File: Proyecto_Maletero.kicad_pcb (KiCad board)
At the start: 2 copper layers, 65.2 x 59 mm, 50 parts, among them J1 DE9_Pins, J2 Conn_01x02, J3 Conn_01x02, J4 Conn_01x03, J5 Conn_01x02, J6 DE9_Pins, J7 Conn_01x04, J9 Conn_01x04, K1 FINDER-34.51, Q2 MMBT5550L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

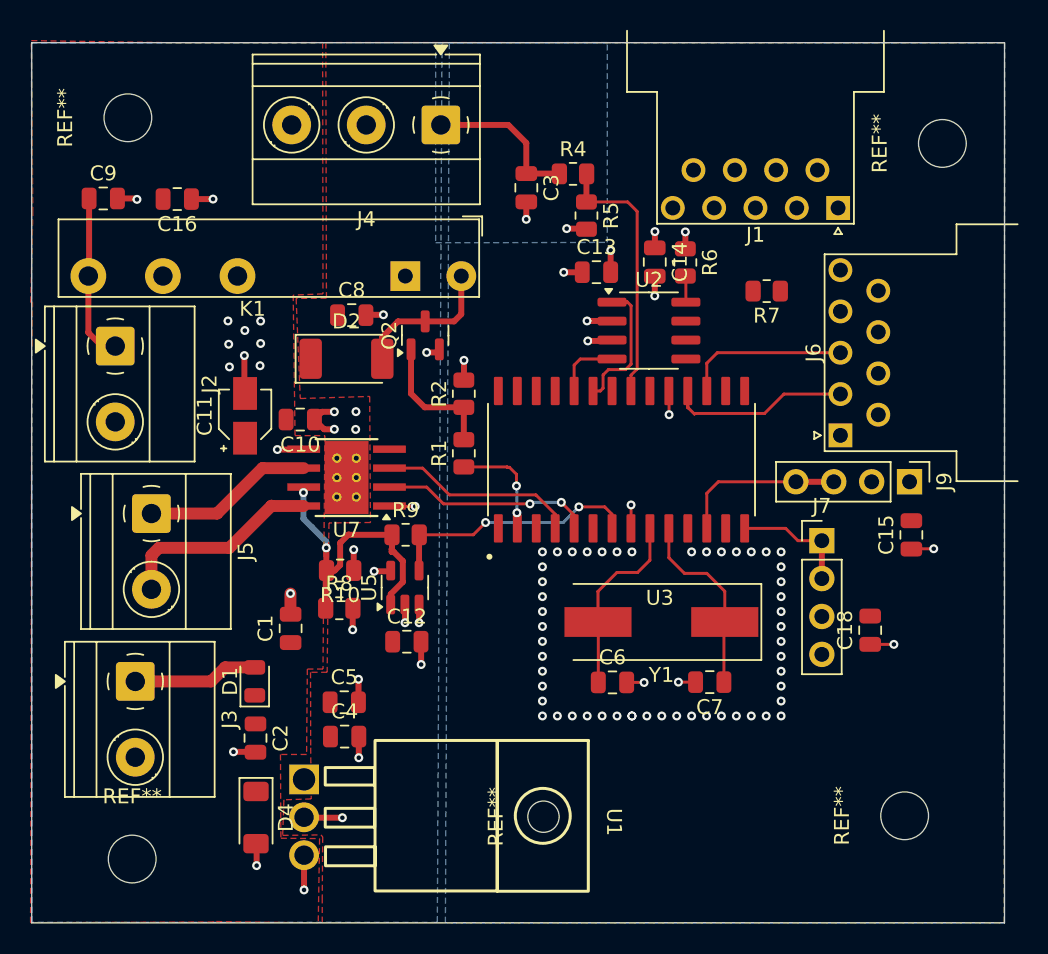
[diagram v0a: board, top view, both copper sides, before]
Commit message: Reglas de diseño, errores 0, separación del transcriver
hay 108 warnings igualmente
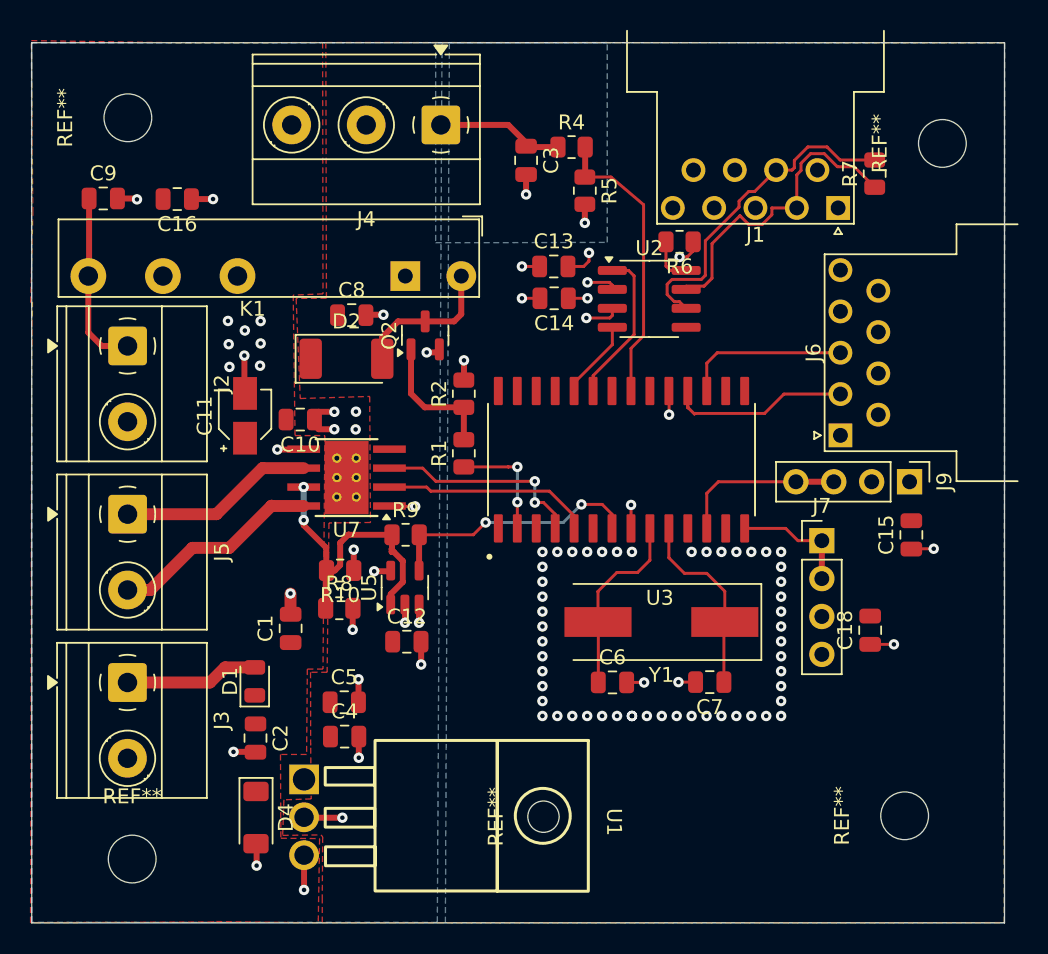
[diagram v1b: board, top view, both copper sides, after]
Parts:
- moved R7 10.7 mm to (165.0, 93.0), turned to 90 degrees
- moved C14 7.17 mm to (143.5, 101.3), turned to 180 degrees
- moved C13 2.89 mm to (143.5, 99.2)
- moved U2 2.12 mm to (149.9, 101.4)
- moved C3 1.84 mm to (141.6, 92.1)
- moved R4 1.80 mm to (144.7, 91.2)
- moved R5 1.67 mm to (145.5, 94.1)
- moved J5 1.60 mm to (114.9, 115.8)
- moved R6 1.43 mm to (151.9, 97.5), turned to 180 degrees
- moved J2 0.82 mm to (114.9, 104.5)
- moved J3 0.53 mm to (114.9, 127.1)
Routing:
- net CAN-: track 0.00 -> 22.3 mm
- net CAN+: track 0.00 -> 21.2 mm
- net Sensor_Pie_12V: track 10.5 -> 8.61 mm
- net Sensor_Pie: track 17.8 -> 19.5 mm
- net Motor+: track 11.5 -> 13.1 mm
- net CAN_TX: track 9.39 -> 10.7 mm
- net Net-(U2-Rs): track 1.80 -> 3.10 mm
- net VCC: track 8.15 -> 9.33 mm
- net GND: track 15.1 -> 16.1 mm
- net CAN_RX: track 4.44 -> 5.33 mm
- net PH_A: track 13.3 -> 14.2 mm, vias 0 -> 2
- net VRth: track 11.2 -> 12.0 mm
- net VBATERIA: track 8.40 -> 8.95 mm
- net PH_B: track 14.1 -> 14.0 mm, vias 2 -> 0

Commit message: Algun cambio
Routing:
- net CAN+: track 21.2 -> 17.4 mm
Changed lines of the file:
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@@
 		(tags "capacitor")
 		(property "Reference" "C16"
-			(at 0 -1.68 0)
+			(at 0 1.82 0)
 			(layer "F.SilkS")
 			(effects
@@
 		(tags "capacitor")
 		(property "Reference" "C3"
-			(at 0 -1.68 90)
+			(at 0.045 1.575 90)
 			(layer "F.SilkS")
 			(effects
@@
 		)
 		(property "Value" "LM1084-5.0"
-			(at 0 1 270)
+			(at 0 0.88 270)
 			(unlocked yes)
 			(layer "F.Fab")
@@
 		(tags "resistor")
 		(property "Reference" "R6"
-			(at 0 -1.65 0)
+			(at -2.568 0.046 0)
 			(layer "F.SilkS")
 			(effects
@@
 		(tags "capacitor")
 		(property "Reference" "C7"
-			(at 0 -1.68 0)
+			(at -2.645 -0.04 0)
 			(layer "F.SilkS")
 			(effects
@@
 		(tags "capacitor")
 		(property "Reference" "C2"
-			(at 0 -1.68 90)
+			(at -0.01 -1.545 90)
 			(layer "F.SilkS")
 			(effects
@@
 		(tags "capacitor")
 		(property "Reference" "C12"
-			(at 0 -1.68 0)
+			(at -0.58 1.83 0)
 			(layer "F.SilkS")
 			(effects
@@
 		(tags "resistor")
 		(property "Reference" "R8"
-			(at 0 -1.65 0)
+			(at 0.0575 1.49 0)
 			(layer "F.SilkS")
 			(effects
@@
 		(tags "SOT TO_SOT_SMD")
 		(property "Reference" "U5"
-			(at 0 -2.4 90)
+			(at 0 -1.56 90)
 			(layer "F.SilkS")
 			(effects
@@
 		(tags "resistor")
 		(property "Reference" "R9"
-			(at 0 -1.65 0)
+			(at 2.5925 0.995 0)
 			(layer "F.SilkS")
 			(effects
@@
 		(tags "THT Terminal Block Phoenix MKDS-1,5-3 pitch 5mm size 15x9.8mm drill 1.3mm pad 2.6mm")
 		(property "Reference" "J4"
-			(at 5 -6.32 0)
+			(at -3.57 2.37 0)
 			(layer "F.SilkS")
 			(effects
@@
 		(tags "Capacitor Electrolytic")
 		(property "Reference" "C11"
-			(at 0 -2.7 90)
+			(at -3.62 -1.015 90)
 			(layer "F.SilkS")
 			(effects
@@
 		(tags "capacitor")
 		(property "Reference" "C6"
-			(at 0 -1.68 0)
+			(at -2.705 0.02 0)
 			(layer "F.SilkS")
 			(effects
@@
 		(tags "resistor")
 		(property "Reference" "R10"
-			(at 0 -1.65 0)
+			(at 3.13 0.12 0)
 			(layer "F.SilkS")
 			(effects
@@
 		(tags "SOIC SO")
 		(property "Reference" "U2"
-			(at 0 -3.4 0)
+			(at -0.42 -3.3502 0)
 			(layer "F.SilkS")
 			(effects
@@
 		(tags "resistor")
 		(property "Reference" "R7"
-			(at 0 -1.65 90)
+			(at -2.756 0.117 90)
 			(layer "F.SilkS")
 			(effects
@@
 		(tags "capacitor")
 		(property "Reference" "C18"
-			(at 0 -1.68 90)
+			(at -3.52 0 90)
 			(layer "F.SilkS")
 			(effects
@@
 		(tags "capacitor")
 		(property "Reference" "C4"
-			(at 0 -1.68 0)
+			(at -2.28 -0.01 90)
 			(layer "F.SilkS")
 			(effects
@@
 	)
 	(segment
-		(start 155.942174 95.784554)
-		(end 156.52395 96.366331)
-		(width 0.2)
-		(layer "F.Cu")
-		(net 8)
-	)
-	(segment
-		(start 154.06798 97.658748)
-		(end 155.942174 95.784554)
-		(width 0.2)
-		(layer "F.Cu")
-		(net 8)
-	)
-	(segment
-		(start 153.537356 100.50618)
-		(end 154.06798 99.975556)
+		(start 160.88 95.23)
+		(end 159.785331 95.23)
 		(width 0.2)
 		(layer "F.Cu")
@@
 	)
 	(segment
-		(start 160.034 92.269281)
-		(end 160.034 92.75953)
+		(start 161.706831 93.8765)
+		(end 161.11 94.473331)
 		(width 0.2)
 		(layer "F.Cu")
@@
 	)
 	(segment
-		(start 160.034 92.75953)
-		(end 159.75 93.04353)
+		(start 154.06798 97.658748)
+		(end 154.06798 100.39202)
 		(width 0.2)
 		(layer "F.Cu")
@@
 	)
 	(segment
-		(start 156.52395 96.366331)
-		(end 157.43605 96.366331)
+		(start 159.785331 95.23)
+		(end 159.75 95.265331)
 		(width 0.2)
 		(layer "F.Cu")
@@
 	)
 	(segment
-		(start 161.59105 91.624331)
-		(end 160.67895 91.624331)
+		(start 161.11 94.473331)
+		(end 161.11 95)
 		(width 0.2)
 		(layer "F.Cu")
@@
 	)
 	(segment
-		(start 152.335 100.7252)
-		(end 152.335 100.50618)
+		(start 161.11 95)
+		(end 160.88 95.23)
 		(width 0.2)
 		(layer "F.Cu")
@@
 	)
 	(segment
-		(start 159.75 93.04353)
-		(end 159.75 95.265331)
+		(start 164.973 93.8765)
+		(end 161.706831 93.8765)
 		(width 0.2)
 		(layer "F.Cu")
@@
 	)
 	(segment
-		(start 158.081 95.721381)
-		(end 158.081 95.265331)
+		(start 155.360397 96.366331)
+		(end 154.06798 97.658748)
 		(width 0.2)
 		(layer "F.Cu")
@@
 	)
 	(segment
-		(start 163.598001 92.501501)
-		(end 162.46822 92.501501)
+		(start 157.543669 96.366331)
+		(end 158.68 95.23)
 		(width 0.2)
 		(layer "F.Cu")
@@
 	)
 	(segment
-		(start 160.67895 91.624331)
-		(end 160.034 92.269281)
+		(start 153.6148 100.7252)
+		(end 152.335 100.7252)
 		(width 0.2)
 		(layer "F.Cu")
@@
 	)
 	(segment
-		(start 164.973 93.8765)
-		(end 163.598001 92.501501)
+		(start 157.543669 96.366331)
+		(end 155.360397 96.366331)
 		(width 0.2)
 		(layer "F.Cu")
@@
 	)
 	(segment
-		(start 154.06798 99.975556)
-		(end 154.06798 97.658748)
+		(start 153.74 100.72)
+		(end 153.62 100.72)
 		(width 0.2)
 		(layer "F.Cu")
@@
 	)
 	(segment
-		(start 157.43605 96.366331)
-		(end 158.081 95.721381)
+		(start 154.06798 100.39202)
+		(end 153.74 100.72)
 		(width 0.2)
 		(layer "F.Cu")
@@
 	)
 	(segment
-		(start 152.335 100.50618)
-		(end 153.537356 100.50618)
+		(start 158.68 95.23)
+		(end 159.714669 95.23)
 		(width 0.2)
 		(layer "F.Cu")
@@
 	)
 	(segment
-		(start 162.46822 92.501501)
-		(end 161.59105 91.624331)
-		(width 0.2)
-		(layer "F.Cu")
-		(net 8)
-	)
-	(segment
-		(start 158.081 95.265331)
+		(start 159.714669 95.23)
 		(end 159.75 95.265331)
 		(width 0.2)
@@
 	)
 	(segment
-		(start 153.618 99.789168)
-		(end 153.618 97.472331)
-		(width 0.2)
-		(layer "F.Cu")
-		(net 12)
-	)
-	(segment
-		(start 159.58402 92.573112)
-		(end 159.431801 92.725331)
+		(start 153.62 100.72)
+		(end 153.6148 100.7252)
 		(width 0.2)
 		(layer "F.Cu")
-		(net 12)
+		(net 8)
 	)
 	(segment
-		(start 152.335 101.9952)
-		(end 151.885 101.5452)
+		(start 160.67895 91.624331)
+		(end 161.734331 91.624331)
 		(width 0.2)
 		(layer "F.Cu")
@@
 	)
 	(segment
-		(start 161.777438 91.174351)
-		(end 160.492562 91.174351)
+		(start 153.618 97.472331)
+		(end 155.51 95.580331)
 		(width 0.2)
 		(layer "F.Cu")
@@
 	)
 	(segment
-		(start 151.387032 100.0562)
-		(end 153.350968 100.0562)
+		(start 161.734331 91.624331)
+		(end 162.1615 92.0515)
 		(width 0.2)
 		(layer "F.Cu")
@@
 	)
 	(segment
-		(start 153.350968 100.0562)
-		(end 153.618 99.789168)
+		(start 151.059 101.789)
+		(end 151.27 102)
 		(width 0.2)
 		(layer "F.Cu")
@@
 	)
 	(segment
-		(start 151.059 100.384232)
-		(end 151.387032 100.0562)
-		(width 0.2)
-		(layer "F.Cu")
-		(net 12)
-	)
-	(segment
-		(start 156.52395 94.164331)
-		(end 156.926 94.164331)
+		(start 157.254669 92.725331)
+		(end 158.365 92.725331)
 		(width 0.2)
 		(layer "F.Cu")
@@
 	)
 	(segment
-		(start 153.618 97.472331)
-		(end 155.879 95.211331)
+		(start 151.387032 100.0562)
+		(end 151.059 100.384232)
 		(width 0.2)
 		(layer "F.Cu")
@@
 	)
 	(segment
-		(start 151.885 101.5452)
-		(end 151.538032 101.5452)
+		(start 155.51 95.580331)
+		(end 155.51 94.47)
 		(width 0.2)
 		(layer "F.Cu")
@@
 	)
 	(segment
-		(start 151.538032 101.5452)
-		(end 151.059 101.066168)
+		(start 159.57795 92.725331)
+		(end 160.67895 91.624331)
 		(width 0.2)
 		(layer "F.Cu")
@@
 	)
 	(segment
-		(start 159.58402 92.082893)
-		(end 159.58402 92.573112)
+		(start 155.51 94.47)
+		(end 157.254669 92.725331)
 		(width 0.2)
 		(layer "F.Cu")
@@
 	)
 	(segment
-		(start 151.059 101.066168)
-		(end 151.059 100.384232)
+		(start 151.059 100.384232)
+		(end 151.059 101.789)
 		(width 0.2)
 		(layer "F.Cu")
@@
 	)
 	(segment
-		(start 164.973 92.0515)
-		(end 162.654587 92.0515)
+		(start 153.618 99.789168)
+		(end 153.350968 100.0562)
 		(width 0.2)
 		(layer "F.Cu")
@@
 	)
 	(segment
-		(start 159.431801 92.725331)
-		(end 158.365 92.725331)
+		(start 151.27 102)
+		(end 151.2748 101.9952)
 		(width 0.2)
 		(layer "F.Cu")
@@
 	)
 	(segment
-		(start 156.926 94.164331)
-		(end 158.365 92.725331)
+		(start 151.2748 101.9952)
+		(end 152.335 101.9952)
 		(width 0.2)
 		(layer "F.Cu")
@@
 	)
 	(segment
-		(start 155.879 95.211331)
-		(end 155.879 94.809281)
+		(start 162.1615 92.0515)
+		(end 164.973 92.0515)
 		(width 0.2)
 		(layer "F.Cu")
@@
 	)
 	(segment
-		(start 160.492562 91.174351)
-		(end 159.58402 92.082893)
+		(start 153.618 97.472331)
+		(end 153.618 99.789168)
 		(width 0.2)
 		(layer "F.Cu")
@@
 	)
 	(segment
-		(start 162.654587 92.0515)
-		(end 161.777438 91.174351)
+		(start 158.365 92.725331)
+		(end 159.57795 92.725331)
 		(width 0.2)
 		(layer "F.Cu")
@@
 	)
 	(segment
-		(start 155.879 94.809281)
-		(end 156.52395 94.164331)
+		(start 153.350968 100.0562)
+		(end 151.387032 100.0562)
 		(width 0.2)
 		(layer "F.Cu")

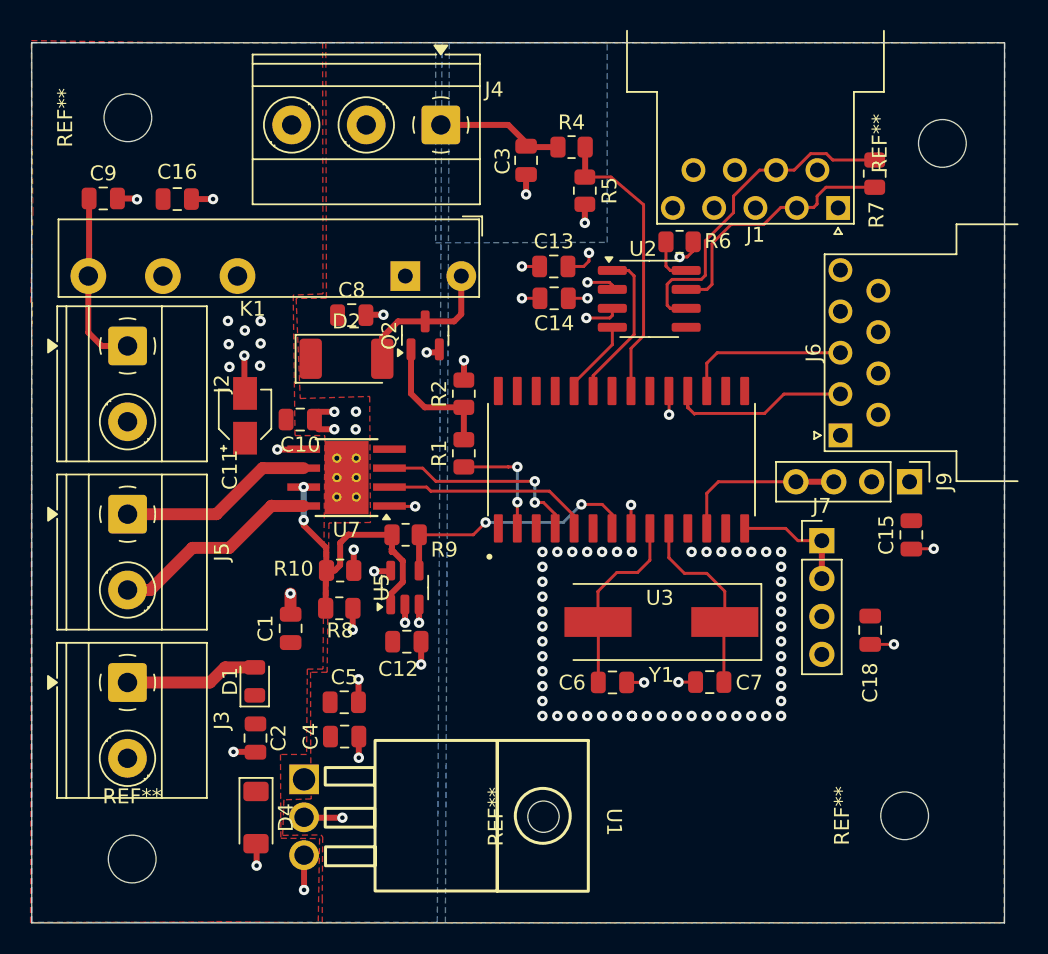
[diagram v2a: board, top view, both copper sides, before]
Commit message: Actualizacion de huella y errores
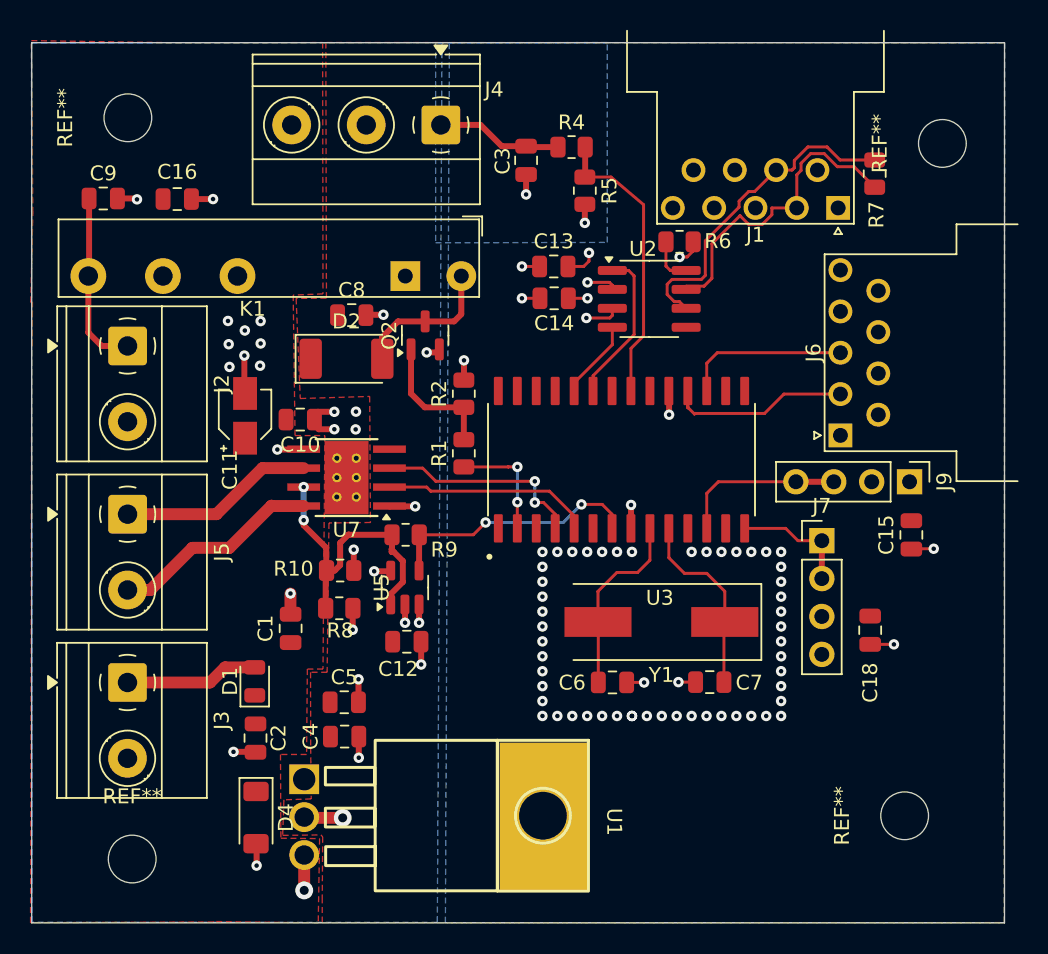
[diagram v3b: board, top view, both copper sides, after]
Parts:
- removed the REF** at (142.8, 136.1)
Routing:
- net CAN+: track 17.4 -> 21.3 mm
